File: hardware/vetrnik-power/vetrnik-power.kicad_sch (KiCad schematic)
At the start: 52 parts, among them J1 12V IN, J2 SHORT, J3 UART, J4 ENABLE, J5 RELAYS, M1 12V / 0,9A max, Q1 BCP56-16, Q2 BC847, Q3 BC846, Q4 BC846, Q5 BC846, Q6 BC846, Q7 BC846, U1 LTV-817, U2 LTV-817, U3 H11L1, U4 H11L1, U5 LTV-817, U6 LTV-847

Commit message: [hardware] Add info about hardware mods
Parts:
- gave numbers to parts that had none: 2
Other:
- note removed: "TODO 4-pin PC fan connector"

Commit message: [hardware] Add info about vetrnik-power fan mod
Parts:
- R2: value 1M -> 3k3
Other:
- note added: "2024-06-27 mod: 3k3 in parallel with R2 (1M)"
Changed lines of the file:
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@@
+    (effects (font (size 1.27 1.27)) (justify left bottom))
+  )
+  (text "2024-06-27 mod:\n3k3 in parallel with R2 (1M)" (at 125.73 40.64 0)
     (effects (font (size 1.27 1.27)) (justify left bottom))
   )
@@
       (effects (font (size 1.27 1.27)) (justify left))
     )
-    (property "Value" "1M" (at 136.398 46.863 0)
-      (effects (font (size 1.27 1.27)) (justify left))
-    )
+    (property "Value" "3k3" (at 136.398 46.863 0)
+      (effects (font (size 1.27 1.27)) (justify left))
+    )

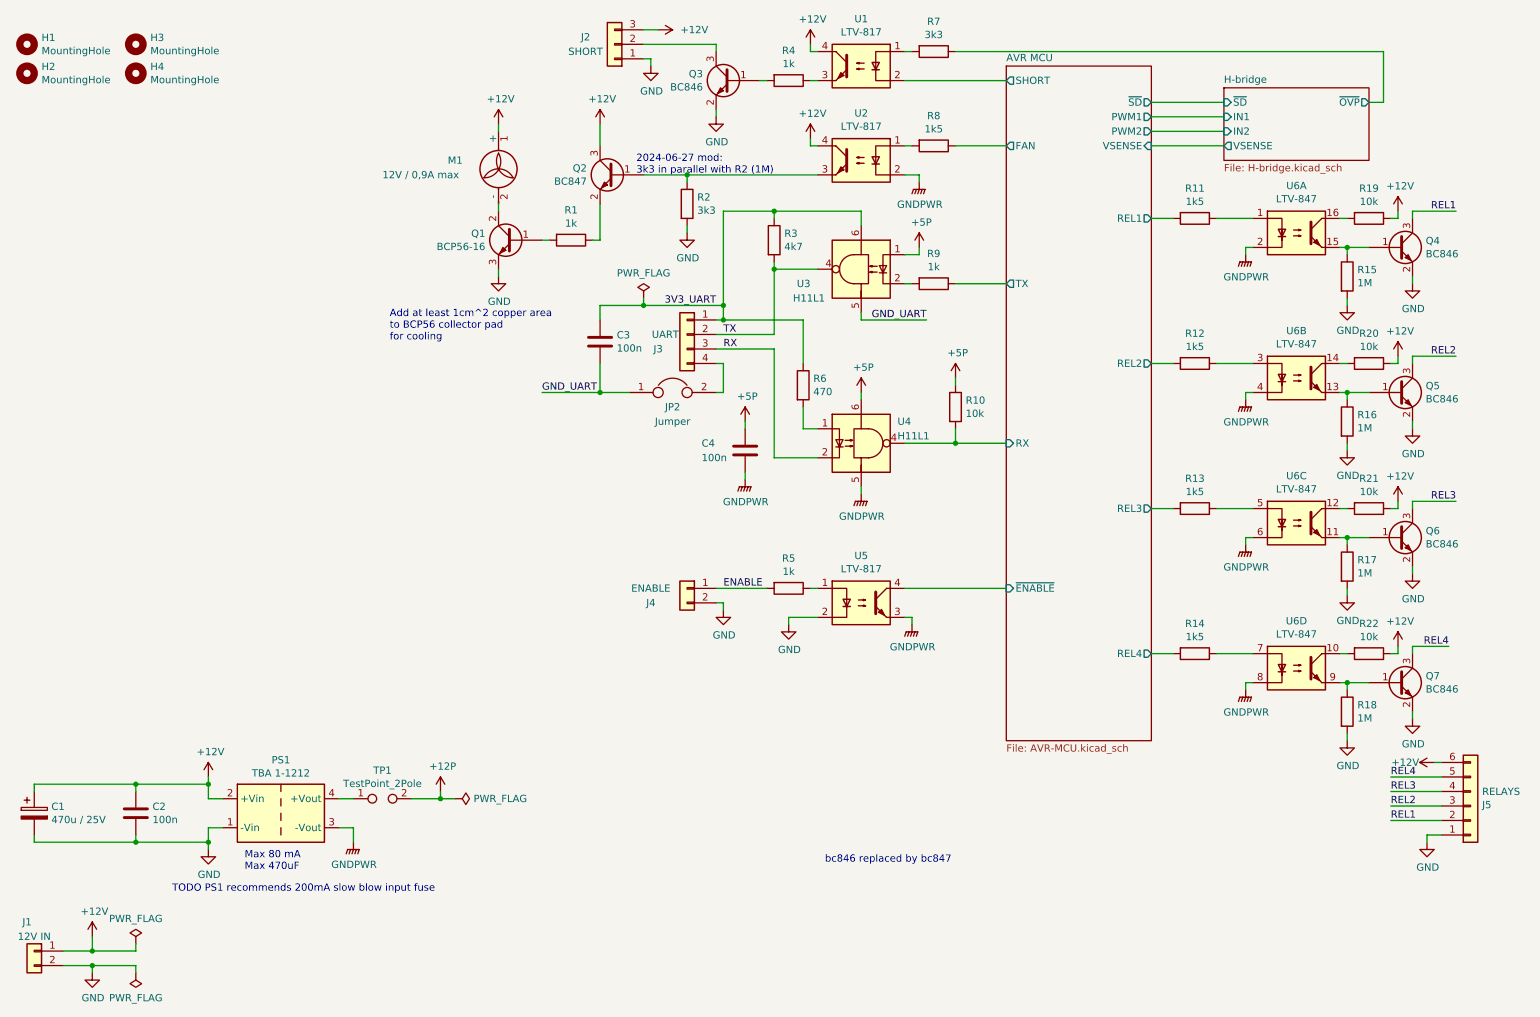
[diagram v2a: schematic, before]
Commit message: [hardware] Clean up vetrnik-power schematic
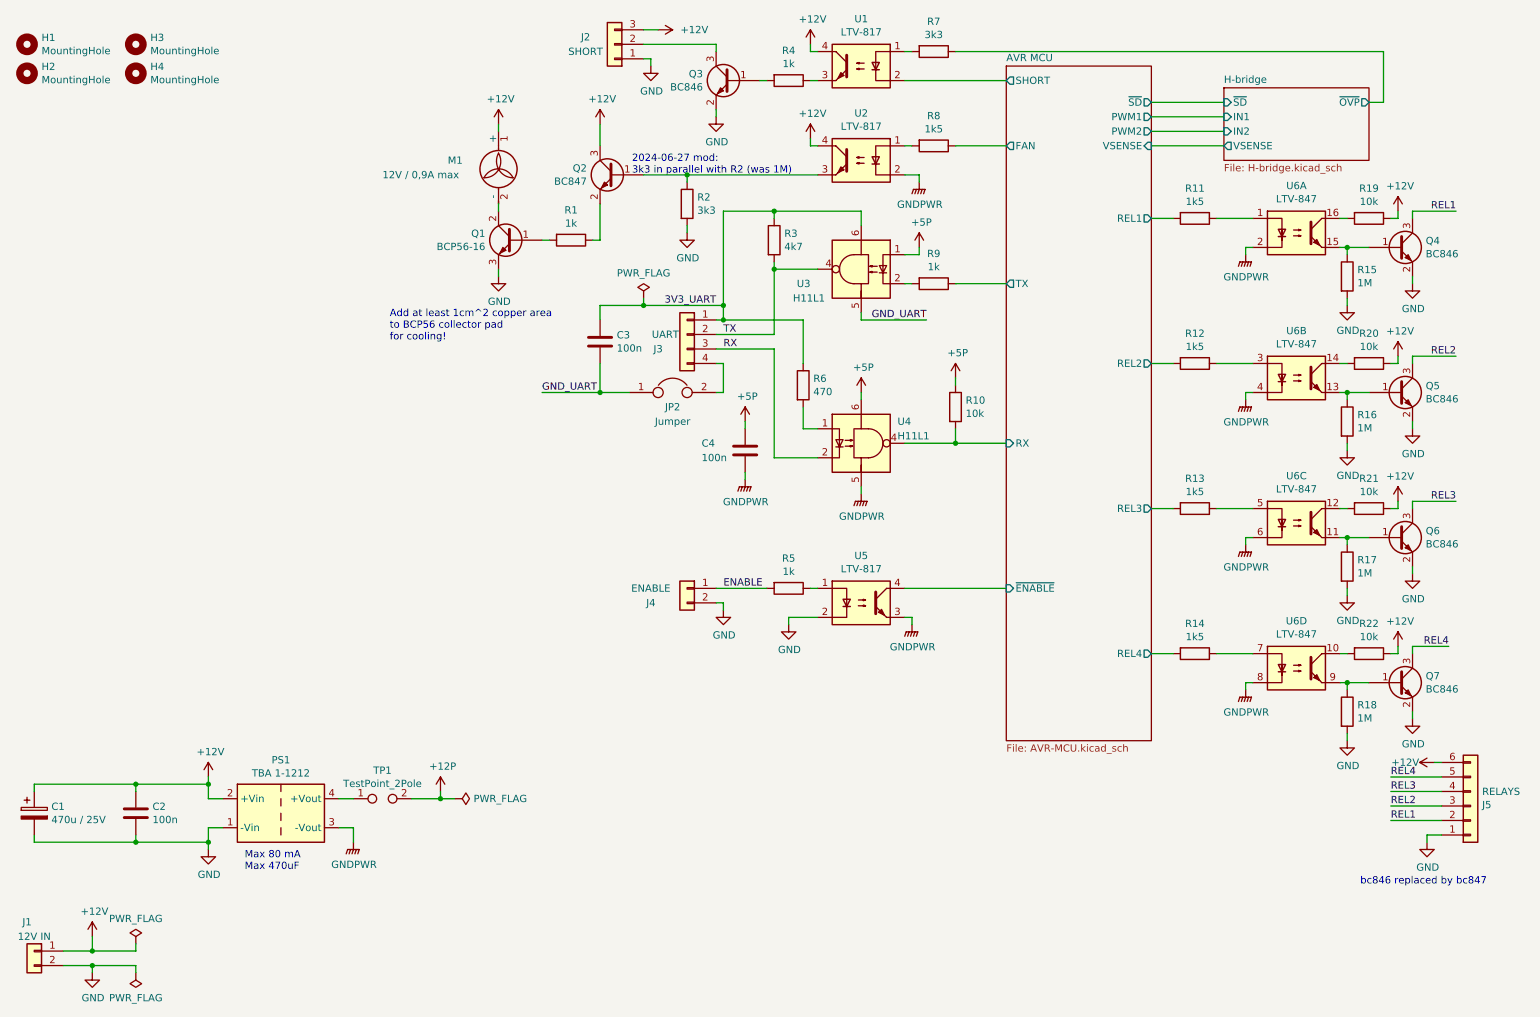
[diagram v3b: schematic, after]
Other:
- note added: "2024-06-27 mod: 3k3 in parallel with R2 (was 1M)"
- note added: "Add at least 1cm^2 copper area to BCP56 collector pad for cooling!"
- note removed: "2024-06-27 mod: 3k3 in parallel with R2 (1M)"
- note removed: "Add at least 1cm^2 copper area to BCP56 collector pad for cooling"
- note removed: "TODO PS1 recommends 200mA slow blow input fuse"
- company: (none) -> Ondřej Sluka
- title: (none) -> vetrnik-power
